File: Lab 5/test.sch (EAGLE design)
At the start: 48 parts, among them J1 FTDI_DEVICERA_SMT, M1 WIRELESS-NRF24L01, U2 GY-521MPU6050, U3 ATMEGA328P_TQFP

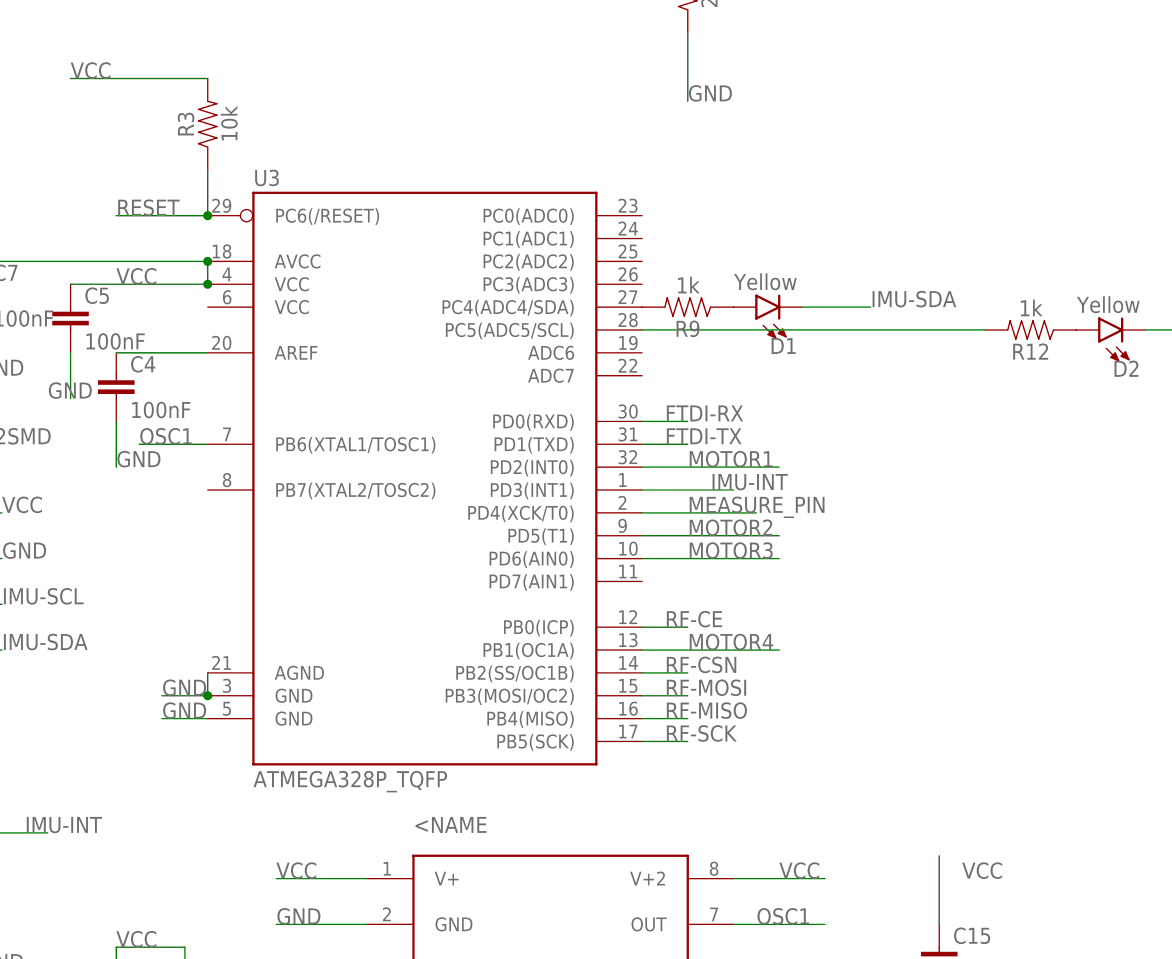
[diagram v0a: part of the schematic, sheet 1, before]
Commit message: Update template file, switch for the right Atmega MCU. Some advice from Arti:   - Everything need to be inside the board (all white frames inside): quadcopter propellers need clearance.   - Nothing under white frame except the Radio Module   - Battery JBT need to have +- on the edge of the PCB   - Mandatory: Top Polygon: VCC, Bottom Polygon: GND; Don't worry about Digital and Analog VCC and GND.
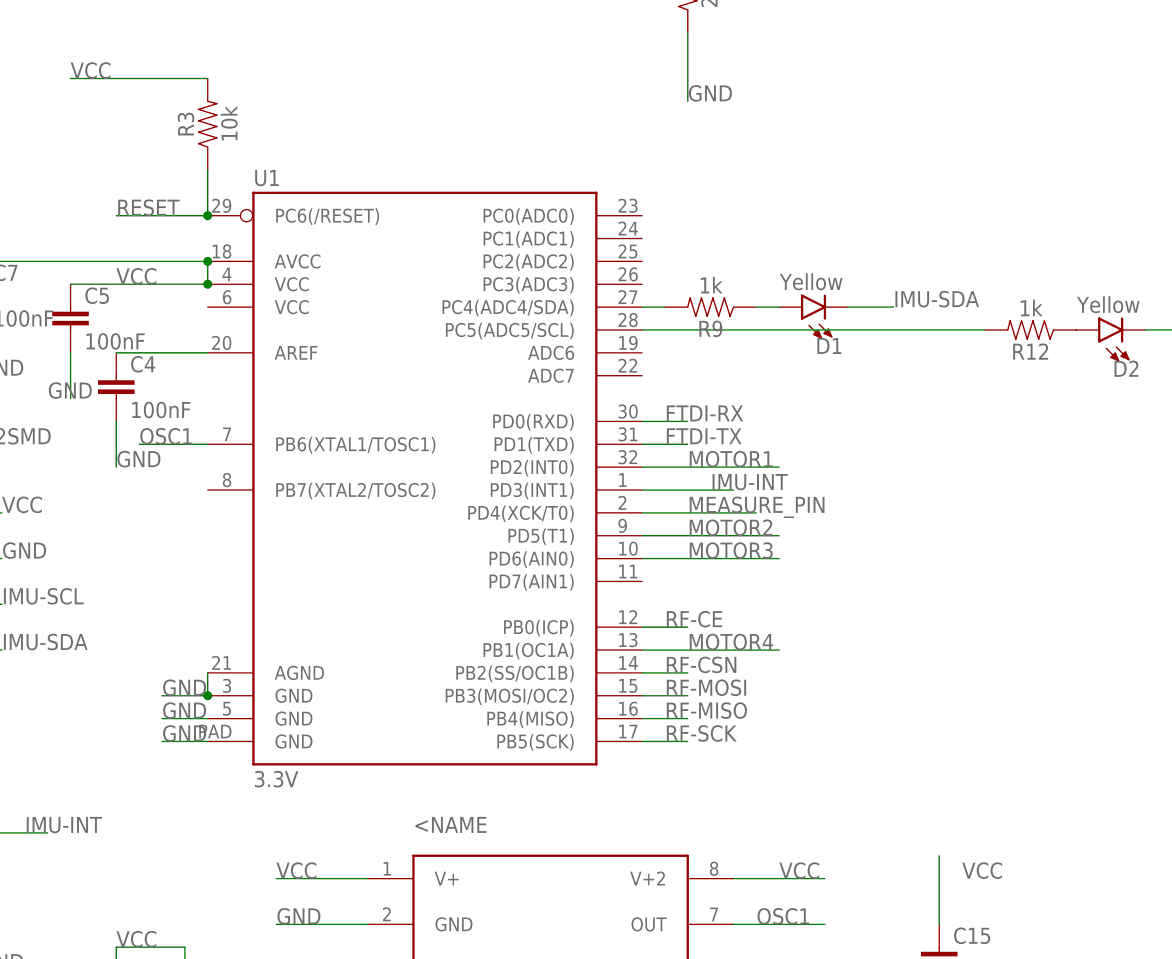
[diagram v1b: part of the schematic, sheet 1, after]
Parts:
- removed U3: ATMEGA328P_TQFP, quad:ATMEGA328P_TQFP
- added U1: 3.3V, SparkFun-DigitalIC:ATMEGA328P_MLFMLF32
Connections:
- removed net N$8 (its old number): R9.2, U3.PC4(ADC4/SDA)
- new net N$3: R9.2, U1.PC4(ADC4/SDA)
- net FTDI-RX: now also U1.PD0(RXD); no longer U3.PD0(RXD)
- net FTDI-TX: now also U1.PD1(TXD); no longer U3.PD1(TXD)
- net GND: now also U1.AGND, U1.GND@3, U1.GND@5, U1.GND@PAD; no longer U3.AGND, U3.GND@3, U3.GND@5
- net IMU-INT: now also U1.PD3(INT1); no longer U3.PD3(INT1)
- net MEASURE_PIN: now also U1.PD4(XCK/T0); no longer U3.PD4(XCK/T0)
- net MOTOR1: now also U1.PD2(INT0); no longer U3.PD2(INT0)
- net MOTOR2: now also U1.PD5(T1); no longer U3.PD5(T1)
- net MOTOR3: now also U1.PD6(AIN0); no longer U3.PD6(AIN0)
- net MOTOR4: now also U1.PB1(OC1A); no longer U3.PB1(OC1A)
- net N$10: now also U1.PC5(ADC5/SCL); no longer U3.PC5(ADC5/SCL)
- net N$2: now also U1.AREF; no longer U3.AREF
- net OSC1: now also U1.PB6(XTAL1/TOSC1); no longer U3.PB6(XTAL1/TOSC1)
- net RESET: now also U1.PC6(/RESET); no longer U3.PC6(/RESET)
- net RF-CE: now also U1.PB0(ICP); no longer U3.PB0(ICP)
- net RF-CSN: now also U1.PB2(SS/OC1B); no longer U3.PB2(SS/OC1B)
- net RF-MISO: now also U1.PB4(MISO); no longer U3.PB4(MISO)
- net RF-MOSI: now also U1.PB3(MOSI/OC2); no longer U3.PB3(MOSI/OC2)
- net RF-SCK: now also U1.PB5(SCK); no longer U3.PB5(SCK)
- net VCC: now also U1.AVCC, U1.VCC@4; no longer U3.AVCC, U3.VCC@4
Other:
- moved on the sheet: D1, R9
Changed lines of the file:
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@@
 </classes>
 <parts>
+<part name="U1" library="SparkFun-DigitalIC" deviceset="ATMEGA328P_MLF" device="MLF32" value="3.3V"/>
 <part name="J1" library="quad" deviceset="FTDI_DEVICE" device="RA_SMT"/>
 <part name="C1" library="SparkFun-Capacitors" deviceset="0.1UF-25V(+80/-20%)(0603)" device="" value="100nF"/>
@@
 <part name="U$3" library="LTC6390" deviceset="LTC6930CMS8-8.19" device="LTC6930CMS8-8.19"/>
 <part name="C15" library="SparkFun-Capacitors" deviceset="0.1UF-25V(+80/-20%)(0603)" device="" value="100nF"/>
-<part name="U3" library="quad" deviceset="ATMEGA328P_TQFP" device="" value="ATMEGA328P_TQFP"/>
 </parts>
 <sheets>
@@
 </plain>
 <instances>
+<instance part="U1" gate="U$1" x="-114.3" y="96.52"/>
 <instance part="J1" gate="G$1" x="-193.04" y="121.92" rot="R180"/>
 <instance part="C1" gate="G$1" x="-187.96" y="111.76"/>
@@
 <instance part="DIODE4" gate="G$1" x="-236.22" y="109.22" rot="MR270"/>
 <instance part="C11" gate="G$1" x="-317.5" y="104.14"/>
-<instance part="R9" gate="G$1" x="-83.82" y="111.76" rot="R180"/>
-<instance part="D1" gate="G$1" x="-76.2" y="111.76" rot="R90"/>
+<instance part="R9" gate="G$1" x="-81.28" y="111.76" rot="R180"/>
+<instance part="D1" gate="G$1" x="-71.12" y="111.76" rot="R90"/>
 <instance part="R12" gate="G$1" x="-45.72" y="109.22" rot="R180"/>
 <instance part="D2" gate="G$1" x="-38.1" y="109.22" rot="R90"/>
 <instance part="U$3" gate="G$1" x="-99.06" y="38.1"/>
 <instance part="C15" gate="G$1" x="-55.88" y="38.1"/>
-<instance part="U3" gate="U$1" x="-111.76" y="91.44"/>
 </instances>
 <busses>
@@
 </segment>
 <segment>
+<pinref part="U1" gate="U$1" pin="GND@3"/>
 <wire x1="-137.16" y1="68.58" x2="-142.24" y2="68.58" width="0.1524" layer="91"/>
 <label x="-142.24" y="68.58" size="1.778" layer="95"/>
+<pinref part="U1" gate="U$1" pin="AGND"/>
 <wire x1="-137.16" y1="71.12" x2="-137.16" y2="68.58" width="0.1524" layer="91"/>
-<pinref part="U3" gate="U$1" pin="AGND"/>
-<pinref part="U3" gate="U$1" pin="GND@3"/>
 <junction x="-137.16" y="68.58"/>
 </segment>
@@
 </segment>
 <segment>
+<pinref part="U1" gate="U$1" pin="GND@5"/>
 <wire x1="-137.16" y1="66.04" x2="-142.24" y2="66.04" width="0.1524" layer="91"/>
 <label x="-142.24" y="66.04" size="1.778" layer="95"/>
-<pinref part="U3" gate="U$1" pin="GND@5"/>
+</segment>
+<segment>
+<pinref part="U1" gate="U$1" pin="GND@PAD"/>
+<wire x1="-137.16" y1="63.5" x2="-142.24" y2="63.5" width="0.1524" layer="91"/>
+<label x="-142.24" y="63.5" size="1.778" layer="95"/>
 </segment>
 <segment>
@@
 </segment>
 <segment>
+<pinref part="U1" gate="U$1" pin="PD0(RXD)"/>
 <wire x1="-88.9" y1="99.06" x2="-83.82" y2="99.06" width="0.1524" layer="91"/>
 <label x="-86.36" y="99.06" size="1.778" layer="95"/>
-<pinref part="U3" gate="U$1" pin="PD0(RXD)"/>
 </segment>
 </net>
@@
 </segment>
 <segment>
+<pinref part="U1" gate="U$1" pin="PD1(TXD)"/>
 <wire x1="-88.9" y1="96.52" x2="-83.82" y2="96.52" width="0.1524" layer="91"/>
 <label x="-86.36" y="96.52" size="1.778" layer="95"/>
-<pinref part="U3" gate="U$1" pin="PD1(TXD)"/>
 </segment>
 </net>
 <net name="RESET" class="0">
 <segment>
+<pinref part="U1" gate="U$1" pin="PC6(/RESET)"/>
 <label x="-147.32" y="121.92" size="1.778" layer="95"/>
 <wire x1="-137.16" y1="121.92" x2="-147.32" y2="121.92" width="0.1524" layer="91"/>
 <pinref part="R3" gate="G$1" pin="1"/>
 <wire x1="-137.16" y1="121.92" x2="-137.16" y2="127" width="0.1524" layer="91"/>
-<pinref part="U3" gate="U$1" pin="PC6(/RESET)"/>
 <junction x="-137.16" y="121.92"/>
 </segment>
@@
 </segment>
 <segment>
+<pinref part="U1" gate="U$1" pin="VCC@4"/>
 <wire x1="-137.16" y1="114.3" x2="-152.4" y2="114.3" width="0.1524" layer="91"/>
 <label x="-147.32" y="114.3" size="1.778" layer="95"/>
 <pinref part="C5" gate="G$1" pin="1"/>
 <pinref part="C7" gate="G$1" pin="1"/>
+<pinref part="U1" gate="U$1" pin="AVCC"/>
 <wire x1="-162.56" y1="116.84" x2="-137.16" y2="116.84" width="0.1524" layer="91"/>
 <wire x1="-137.16" y1="116.84" x2="-137.16" y2="114.3" width="0.1524" layer="91"/>
-<pinref part="U3" gate="U$1" pin="AVCC"/>
 <junction x="-137.16" y="116.84"/>
-<pinref part="U3" gate="U$1" pin="VCC@4"/>
 <junction x="-137.16" y="114.3"/>
 </segment>
@@
 </segment>
 <segment>
+<pinref part="U1" gate="U$1" pin="PB0(ICP)"/>
 <wire x1="-88.9" y1="76.2" x2="-83.82" y2="76.2" width="0.1524" layer="91"/>
 <label x="-86.36" y="76.2" size="1.778" layer="95"/>
-<pinref part="U3" gate="U$1" pin="PB0(ICP)"/>
 </segment>
 </net>
@@
 </segment>
 <segment>
+<pinref part="U1" gate="U$1" pin="PB2(SS/OC1B)"/>
 <wire x1="-88.9" y1="71.12" x2="-83.82" y2="71.12" width="0.1524" layer="91"/>
 <label x="-86.36" y="71.12" size="1.778" layer="95"/>
-<pinref part="U3" gate="U$1" pin="PB2(SS/OC1B)"/>
 </segment>
 </net>
@@
 </segment>
 <segment>
+<pinref part="U1" gate="U$1" pin="PB5(SCK)"/>
 <wire x1="-88.9" y1="63.5" x2="-83.82" y2="63.5" width="0.1524" layer="91"/>
 <label x="-86.36" y="63.5" size="1.778" layer="95"/>
-<pinref part="U3" gate="U$1" pin="PB5(SCK)"/>
 </segment>
 </net>
@@
 </segment>
 <segment>
+<pinref part="U1" gate="U$1" pin="PB3(MOSI/OC2)"/>
 <wire x1="-88.9" y1="68.58" x2="-83.82" y2="68.58" width="0.1524" layer="91"/>
 <label x="-86.36" y="68.58" size="1.778" layer="95"/>
-<pinref part="U3" gate="U$1" pin="PB3(MOSI/OC2)"/>
 </segment>
 </net>
@@
 </segment>
 <segment>
+<pinref part="U1" gate="U$1" pin="PB4(MISO)"/>
 <wire x1="-88.9" y1="66.04" x2="-83.82" y2="66.04" width="0.1524" layer="91"/>
 <label x="-86.36" y="66.04" size="1.778" layer="95"/>
-<pinref part="U3" gate="U$1" pin="PB4(MISO)"/>
 </segment>
 </net>
@@
 <segment>
 <pinref part="D1" gate="G$1" pin="C"/>
-<wire x1="-71.12" y1="111.76" x2="-63.5" y2="111.76" width="0.1524" layer="91"/>
-<label x="-63.5" y="111.76" size="1.778" layer="95"/>
+<wire x1="-66.04" y1="111.76" x2="-60.96" y2="111.76" width="0.1524" layer="91"/>
+<label x="-60.96" y="111.76" size="1.778" layer="95"/>
 </segment>
 </net>
@@
 </segment>
 <segment>
+<pinref part="U1" gate="U$1" pin="PD2(INT0)"/>
 <wire x1="-88.9" y1="93.98" x2="-73.66" y2="93.98" width="0.1524" layer="91"/>
 <label x="-83.82" y="93.98" size="1.778" layer="95"/>
-<pinref part="U3" gate="U$1" pin="PD2(INT0)"/>
 </segment>
 </net>
@@
 </segment>
 <segment>
+<pinref part="U1" gate="U$1" pin="PD5(T1)"/>
 <wire x1="-88.9" y1="86.36" x2="-73.66" y2="86.36" width="0.1524" layer="91"/>
 <label x="-83.82" y="86.36" size="1.778" layer="95"/>
-<pinref part="U3" gate="U$1" pin="PD5(T1)"/>
 </segment>
 </net>
@@
 </segment>
 <segment>
+<pinref part="U1" gate="U$1" pin="PD6(AIN0)"/>
 <wire x1="-88.9" y1="83.82" x2="-73.66" y2="83.82" width="0.1524" layer="91"/>
 <label x="-83.82" y="83.82" size="1.778" layer="95"/>
-<pinref part="U3" gate="U$1" pin="PD6(AIN0)"/>
 </segment>
 </net>
@@
 </segment>
 <segment>
+<pinref part="U1" gate="U$1" pin="PB1(OC1A)"/>
 <wire x1="-88.9" y1="73.66" x2="-73.66" y2="73.66" width="0.1524" layer="91"/>
 <label x="-83.82" y="73.66" size="1.778" layer="95"/>
-<pinref part="U3" gate="U$1" pin="PB1(OC1A)"/>
 </segment>
 </net>
@@
 <segment>
 <pinref part="C4" gate="G$1" pin="1"/>
+<pinref part="U1" gate="U$1" pin="AREF"/>
 <wire x1="-147.32" y1="106.68" x2="-137.16" y2="106.68" width="0.1524" layer="91"/>
-<pinref part="U3" gate="U$1" pin="AREF"/>
 </segment>
 </net>
@@
 </segment>
 <segment>
+<pinref part="U1" gate="U$1" pin="PD4(XCK/T0)"/>
 <wire x1="-88.9" y1="88.9" x2="-76.2" y2="88.9" width="0.1524" layer="91"/>
 <label x="-83.82" y="88.9" size="1.778" layer="95"/>
-<pinref part="U3" gate="U$1" pin="PD4(XCK/T0)"/>
 </segment>
 </net>
@@
 <net name="OSC1" class="0">
 <segment>
+<pinref part="U1" gate="U$1" pin="PB6(XTAL1/TOSC1)"/>
 <wire x1="-137.16" y1="96.52" x2="-144.78" y2="96.52" width="0.1524" layer="91"/>
 <label x="-144.78" y="96.52" size="1.778" layer="95"/>
-<pinref part="U3" gate="U$1" pin="PB6(XTAL1/TOSC1)"/>
 </segment>
 <segment>
@@
 </segment>
 <segment>
+<pinref part="U1" gate="U$1" pin="PD3(INT1)"/>
 <wire x1="-88.9" y1="91.44" x2="-78.74" y2="91.44" width="0.1524" layer="91"/>
 <label x="-81.28" y="91.44" size="1.778" layer="95"/>
-<pinref part="U3" gate="U$1" pin="PD3(INT1)"/>
 </segment>
 </net>
@@
 </segment>
 </net>
+<net name="N$3" class="0">
+<segment>
+<pinref part="U1" gate="U$1" pin="PC4(ADC4/SDA)"/>
+<pinref part="R9" gate="G$1" pin="2"/>
+<wire x1="-88.9" y1="111.76" x2="-86.36" y2="111.76" width="0.1524" layer="91"/>
+</segment>
+</net>
+<net name="N$8" class="0">
+<segment>
+<pinref part="R9" gate="G$1" pin="1"/>
+<pinref part="D1" gate="G$1" pin="A"/>
+<wire x1="-76.2" y1="111.76" x2="-73.66" y2="111.76" width="0.1524" layer="91"/>
+</segment>
+</net>
 <net name="N$9" class="0">
 <segment>
@@
 <net name="N$10" class="0">
 <segment>
+<pinref part="U1" gate="U$1" pin="PC5(ADC5/SCL)"/>
 <pinref part="R12" gate="G$1" pin="2"/>
 <wire x1="-88.9" y1="109.22" x2="-50.8" y2="109.22" width="0.1524" layer="91"/>
-<pinref part="U3" gate="U$1" pin="PC5(ADC5/SCL)"/>
-</segment>
-</net>
-<net name="N$3" class="0">
-<segment>
-<pinref part="R9" gate="G$1" pin="1"/>
-<pinref part="D1" gate="G$1" pin="A"/>
-</segment>
-</net>
-<net name="N$8" class="0">
-<segment>
-<pinref part="R9" gate="G$1" pin="2"/>
-<pinref part="U3" gate="U$1" pin="PC4(ADC4/SDA)"/>
-</segment>
-</net>
+</segment>
+</net>
